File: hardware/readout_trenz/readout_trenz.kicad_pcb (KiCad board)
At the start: 6 copper layers, 383 parts, among them J1 Conn_Coaxial, J10 ERM8-060-05.0-L-DV, J11 ERM8-060-05.0-L-DV, J12 ERM8-060-05.0-L-DV, J13 ERM8-060-05.0-L-DV, J14 Digilent JTAG header, J15 SparkfunFT232RL, J16 TrenzSFP+cage, J17 Trenz_Module, J18 Conn_02x05_Odd_Even, J19 BNC, J2 Conn_Coaxial, J3 Conn_Coaxial_Power, J4 Conn_02x05_Odd_Even, J5 Conn_01x10, J6 Conn_01x10, J7 BNC, J8 ERM8-060-05.0-L-DV, J9 ERM8-060-05.0-L-DV, Q1 DMN67D7L, Q2 DMN67D7L, Q3 DMN67D7L, Q4 DMN67D7L, Q5 DMN67D7L, Q6 DMN67D7L, Q7 DMN67D7L, U1 SN74AXC2T45DCTR, U10 NLSV8T244, U11 NLSV8T244, U12 DS90LV027A, U13 ADS7955, U14 REF5025, U15 SN74AXC2T45DCTR, U16 CITIROC1A, U17 SN74AXC2T45DCTR, U18 NLSV8T244, U19 NLSV8T244, U2 LP2985-5.0, U20 DS90LV027A, U21 ADS7955, U22 REF5025, U23 SN74AXC2T45DCTR, U3 NCP718xSN180, U4 NCP718xSN180, U5 LT1963AxQ-3.3, U6 LT1963AxQ-3.3, U7 LT1963AxQ-3.3, U8 CITIROC1A, U9 SN74AXC2T45DCTR

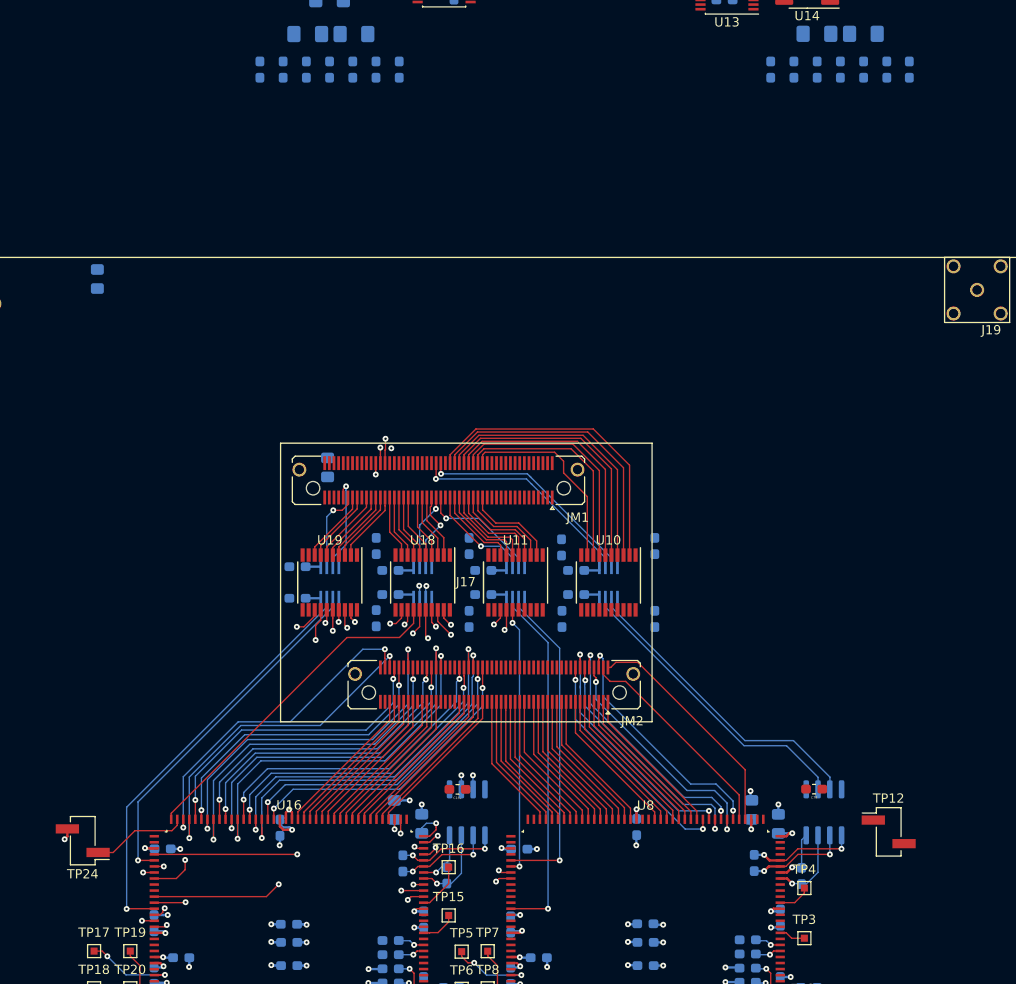
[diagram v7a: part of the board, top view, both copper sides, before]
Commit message: Readout Layout in progress
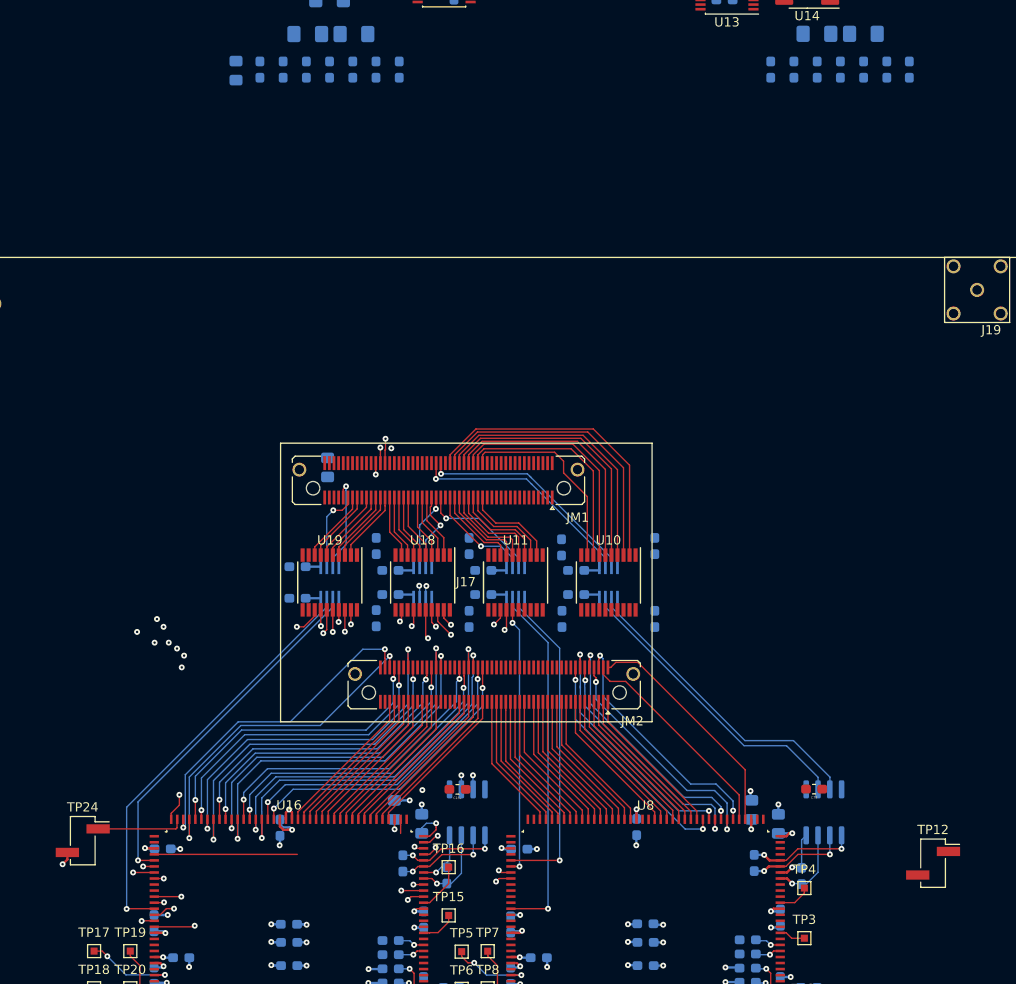
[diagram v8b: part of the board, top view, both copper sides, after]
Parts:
- TP12, TP24: footprint Connector_PinHeader_2.54mm:PinHeader_1x02_P2.54mm_Vertical_SMD_Pin1Left -> Connector_PinHeader_2.54mm:PinHeader_1x02_P2.54mm_Vertical_SMD_Pin1Right
- moved R58 27.0 mm to (342.9, 79.9)
- moved TP12 5.85 mm to (418.0, 165.2)
- turned TP24 to 0 degrees
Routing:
- net Net-(U16-Pad124): track 46.9 -> 15.4 mm, vias 2 -> 0
- net Net-(U16-Pad82): track 27.0 -> 1.53 mm, vias 2 -> 0
- net Net-(U16-Pad120): track 36.7 -> 49.9 mm, vias 0 -> 3
- net Net-(U16-Pad127): track 37.4 -> 50.2 mm, vias 2 -> 3
- net Net-(U16-Pad136): track 45.3 -> 55.4 mm, vias 2 -> 3
- net Net-(U16-Pad135): track 46.4 -> 55.7 mm, vias 2 -> 3
- net Net-(U16-Pad132): track 41.4 -> 49.8 mm, vias 2 -> 3
- net Net-(U16-Pad128): track 37.9 -> 45.6 mm, vias 2 -> 3
- net Net-(U16-Pad134): track 44.3 -> 51.7 mm, vias 2 -> 3
- net Net-(U16-Pad126): track 39.9 -> 47.1 mm, vias 2 -> 3
- net Net-(U16-Pad131): track 49.3 -> 55.3 mm, vias 2 -> 3
- net Net-(TP24-Pad1): track 10.4 -> 9.43 mm
